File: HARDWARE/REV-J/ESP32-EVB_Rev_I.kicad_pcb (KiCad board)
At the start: 2 copper layers, 75.2 x 74.7 mm, 155 parts, among them CON1 TB3 DG306-5.0-3P, CON2 TB3 DG306-5.0-3P, Q1 BC817-40(SOT23), Q2 BC817-40(SOT23), Q3 Q12MHz/20pF/30ppm/2P/HC-49SM(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, Q4 BC817-40(SOT23), Q5 BC817-40(SOT23), Q7 BC817-40(SOT23), U1 BL4054B-42TPRN(SOT23-5), U10 BAT54C(SOT23-3), U2 SY8089AAAC(SOT23-5), U3 ESP-WROOM-32, U4 LAN8710A-EZC(QFN32), U5 CH340T(SSOP20W), U6 MCP2562-E/SN(SOIC-8_150mil), U7 RPM7236-H8, U8 NCP303LSN27T1G(SOT-23-5), U9 BAT54C(SOT23-3)

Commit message: Update 434121043836 (rev1).stp, 5040771891.stp, and 173 more files...
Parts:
- removed C/M: Closed(1-2)/Opened(2-3), OLIMEX_Jumpers-FP:SJ_2_SMALL_12_TIED
- added 5.0V/3.3V2: Closed(1-2)/Opened(2-3), OLIMEX_Jumpers-FP:SJ_2_SMALL_12_TIED, F.Cu at (127.4, 114.0)
- CAN_T1: moved to F.Cu
- R47: moved to B.Cu
- moved 5.0V/3.3V1 4.40 mm to (119.9, 112.8), turned to 180 degrees
- moved R13 2.99 mm to (133.3, 109.7), turned to 270 degrees
- moved CAN_T1 1.74 mm to (134.3, 112.6)
- moved R12 1.49 mm to (134.2, 114.8), turned to 180 degrees
- moved R47 1.30 mm to (135.5, 112.7)
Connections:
- 5.0V/3.3V1 pad 2: Net-(5.0V/3.3V1-Pad2) -> mb+
- C25 pad 2: Net-(5.0V/3.3V1-Pad2) -> mb+
- C26 pad 2: Net-(5.0V/3.3V1-Pad2) -> mb+
- R12 pad 1: GND -> /CANH
- R12 pad 2: /CANH -> GND
- R13 pad 1: /CANL -> mb+
- R13 pad 2: vm -> /CANL
- R48 pad 1: vm -> mb+
- R48 pad 2: Net-(5.0V/3.3V1-Pad2) -> mb+
- R49 pad 1: vm -> mb+
- U6 pad 2: GND -> Net-(U6-Pad2)
- U6 pad 3: Net-(5.0V/3.3V1-Pad2) -> Net-(U6-Pad2)
- U6 pad 8: vm -> mb+
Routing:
- net mb+: track 0.00 -> 26.3 mm, vias 0 -> 3
- net Net-(5.0V/3.3V1-Pad2): track 13.0 -> 0.00 mm, vias 1 -> 0
- net Net-(U6-Pad2): track 0.00 -> 8.96 mm
- net GND: track 995.9 -> 1002.4 mm, vias 133 -> 132
- net vm: track 5.82 -> 0.00 mm
- net /CANL: track 18.9 -> 22.5 mm, vias 1 -> 0
- net /GPI35/CAN-RX: track 111.3 -> 114.6 mm
- net +5V: track 140.2 -> 138.0 mm
- net Net-(5.0V/3.3V2-Pad2): track 3.97 -> 2.22 mm
- net +3V3: track 246.0 -> 244.3 mm, vias 15 -> 14
- net /CANH: track 27.0 -> 25.9 mm

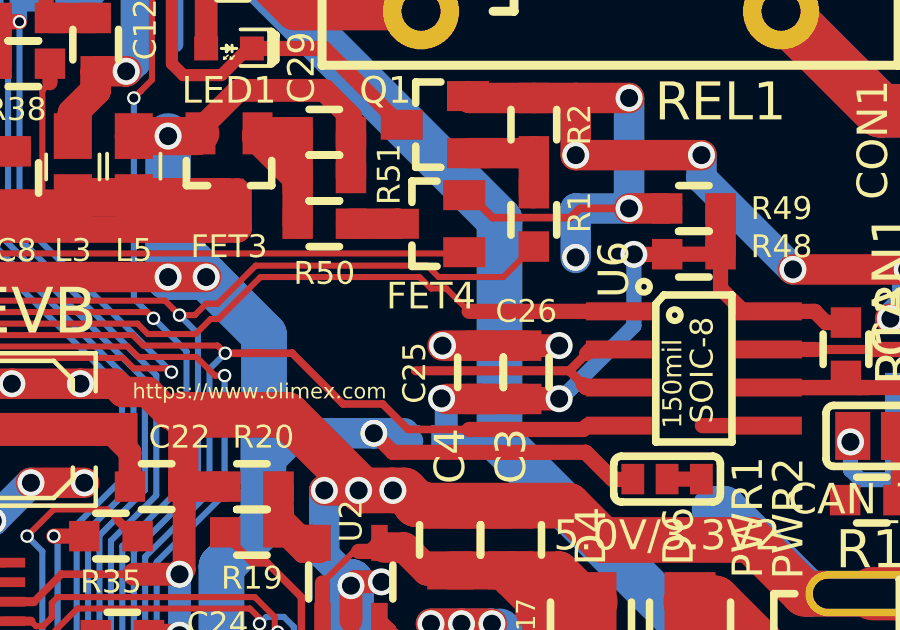
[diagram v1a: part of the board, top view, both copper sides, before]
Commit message: Update ESP32-EVB_Rev_I-cache.lib, ESP32-EVB_Rev_I.kicad_pcb, and 3 more files...
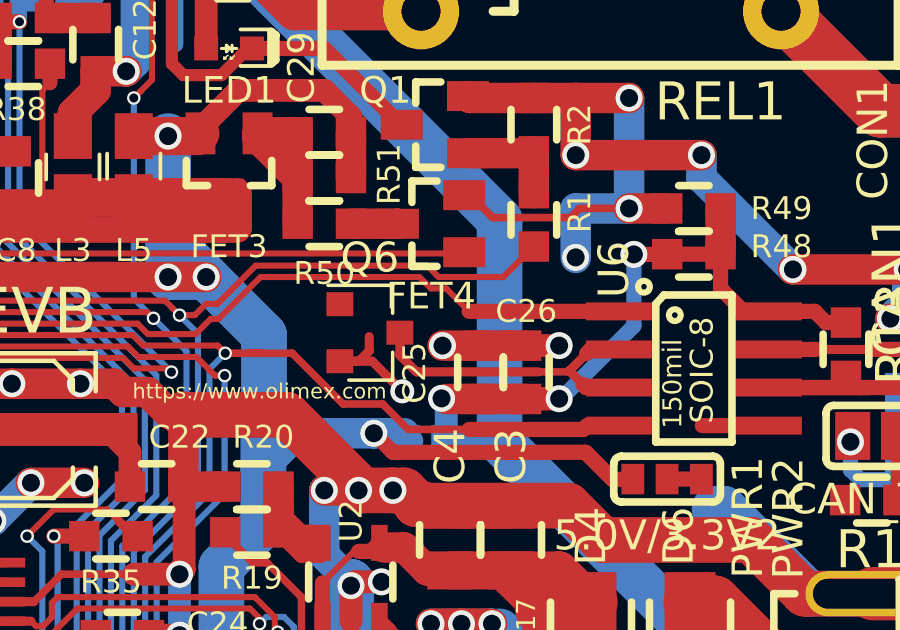
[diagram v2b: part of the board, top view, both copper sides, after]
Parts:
- added Q6: BC817, Package_TO_SOT_SMD:SOT-23, F.Cu at (117.5, 109.2)
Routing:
- net GND: track 1002.4 -> 1006.5 mm, vias 132 -> 133
- net Net-(Q6-Pad3): track 8.96 -> 10.5 mm

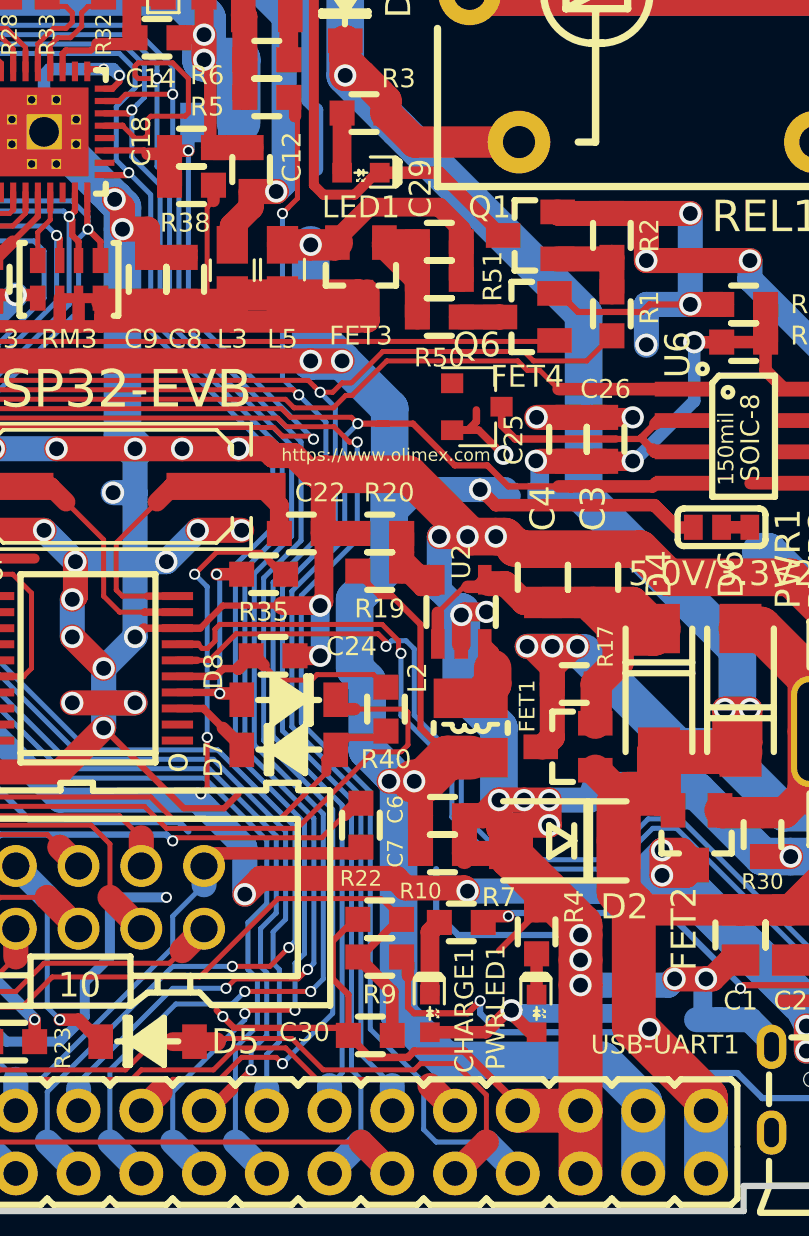
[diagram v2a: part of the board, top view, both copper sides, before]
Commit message: fix auto control flow modbus
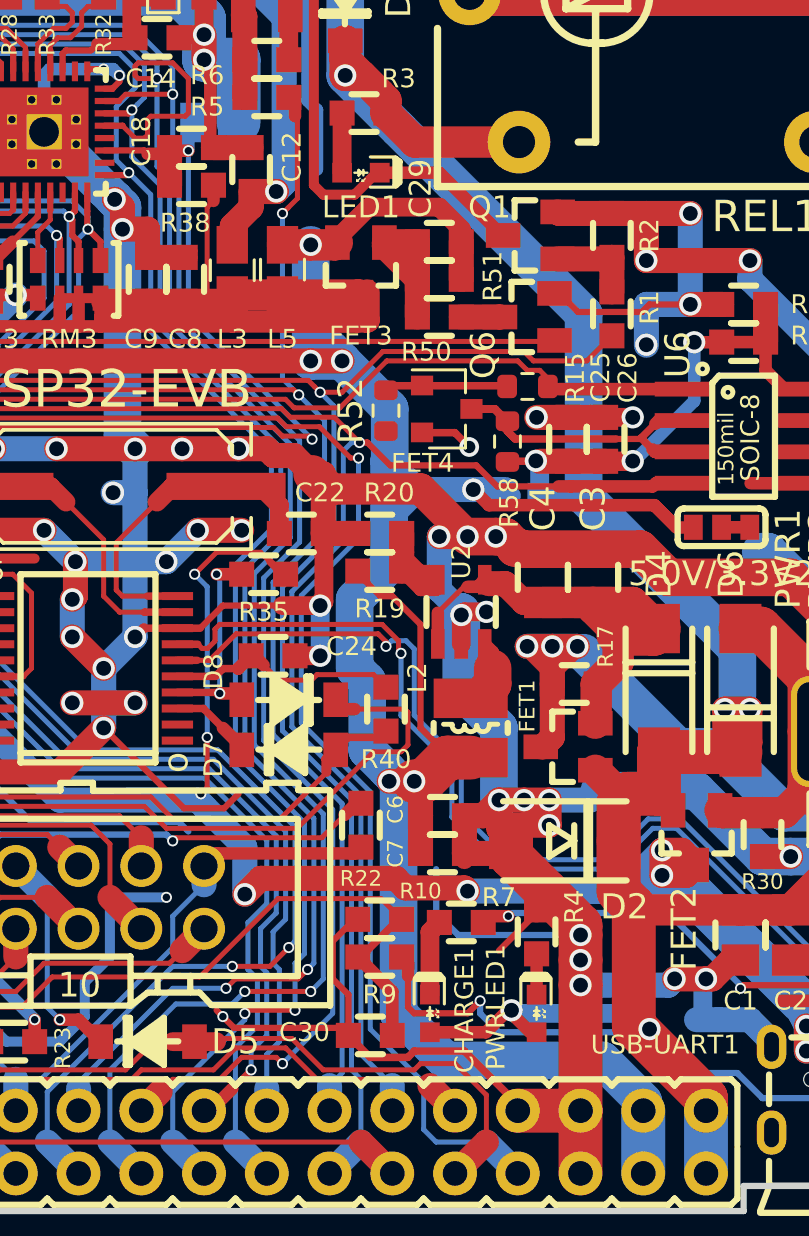
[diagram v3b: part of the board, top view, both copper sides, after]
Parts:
- added R15: R, Resistor_SMD:R_0603_1608Metric, F.Cu at (119.5, 108.3)
- added R52: R, Resistor_SMD:R_0603_1608Metric, F.Cu at (113.8, 109.3)
- added R58: R, Resistor_SMD:R_0603_1608Metric, F.Cu at (118.7, 110.6)
- moved Q6 1.22 mm to (116.2, 109.3)
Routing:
- net Net-(Q6-Pad1): track 0.00 -> 4.72 mm
- net Net-(Q6-Pad3): track 10.5 -> 14.7 mm
- net /GPI35/CAN-RX: track 114.6 -> 112.8 mm
- net GND: track 1006.5 -> 1005.0 mm
- net mb+: track 26.3 -> 27.5 mm
- net /GPIO5/CAN-TX: track 109.7 -> 110.3 mm

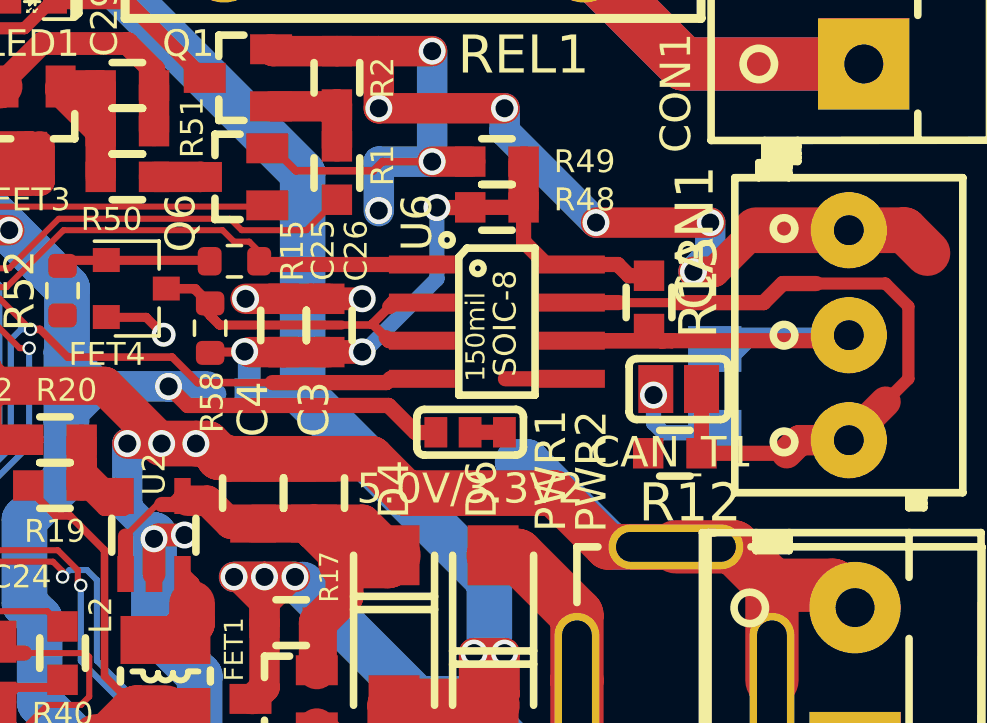
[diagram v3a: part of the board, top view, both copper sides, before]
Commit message: done modbus 485
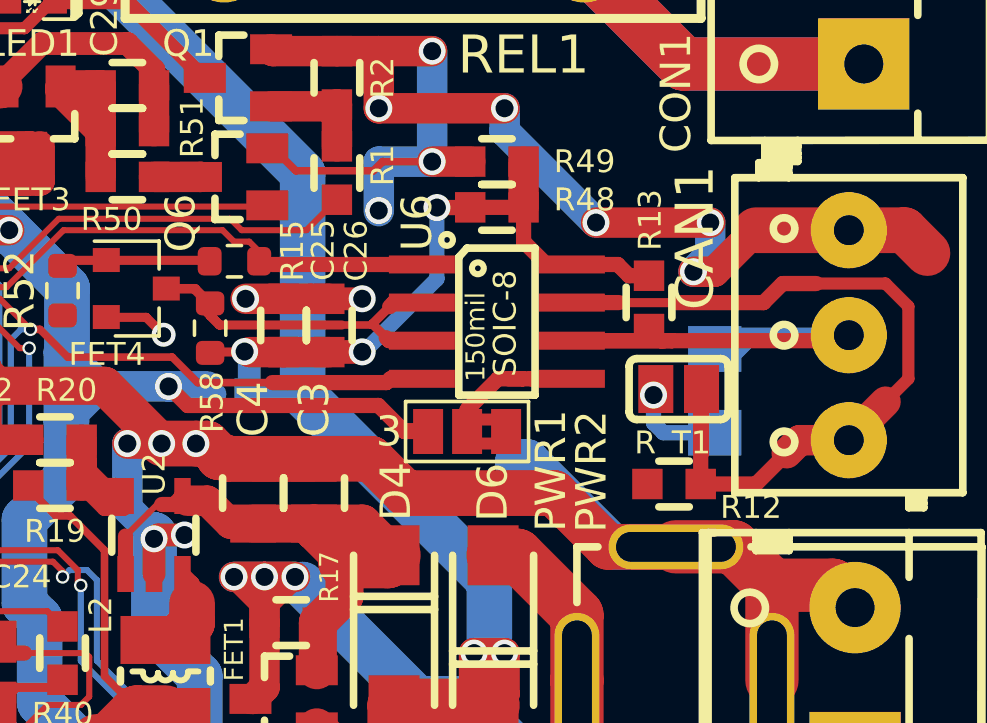
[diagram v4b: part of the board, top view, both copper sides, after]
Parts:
- removed 5.0V/3.3V2: Closed(1-2)/Opened(2-3), OLIMEX_Jumpers-FP:SJ_2_SMALL_12_TIED
- removed CAN_T1: Opened, OLIMEX_Jumpers-FP:SJ
- added JP1: SolderJumper_3_Bridged12, Jumper:SolderJumper-3_P1.3mm_Bridged2Bar12_Pad1.0x1.5mm_NumberLabels, F.Cu at (127.3, 114.0)
- added R_T1: Opened, OLIMEX_Jumpers-FP:SJ, F.Cu at (134.3, 112.6)
- moved R12 1.03 mm to (134.2, 115.8)
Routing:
- net /CANH: track 25.9 -> 30.1 mm
- net Net-(JP1-Pad2): track 2.22 -> 5.14 mm
- net +3V3: track 244.6 -> 243.8 mm

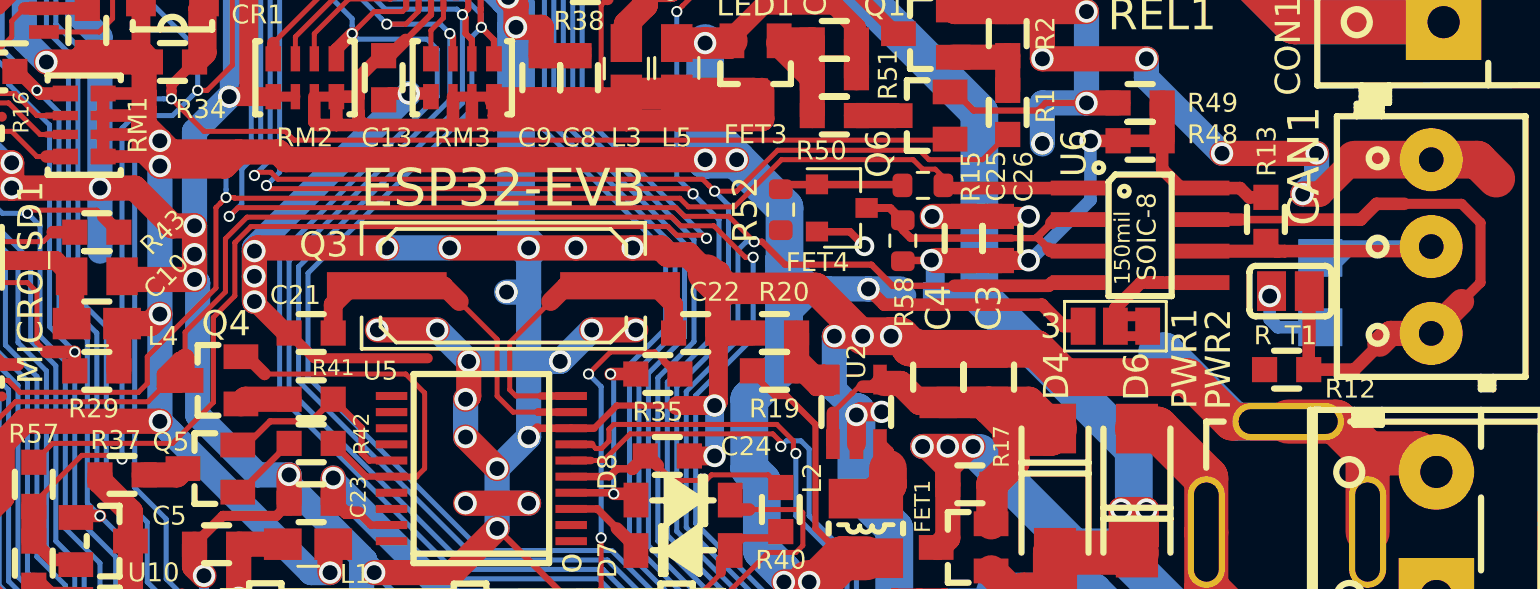
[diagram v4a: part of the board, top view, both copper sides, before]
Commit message: re-position micro usb port
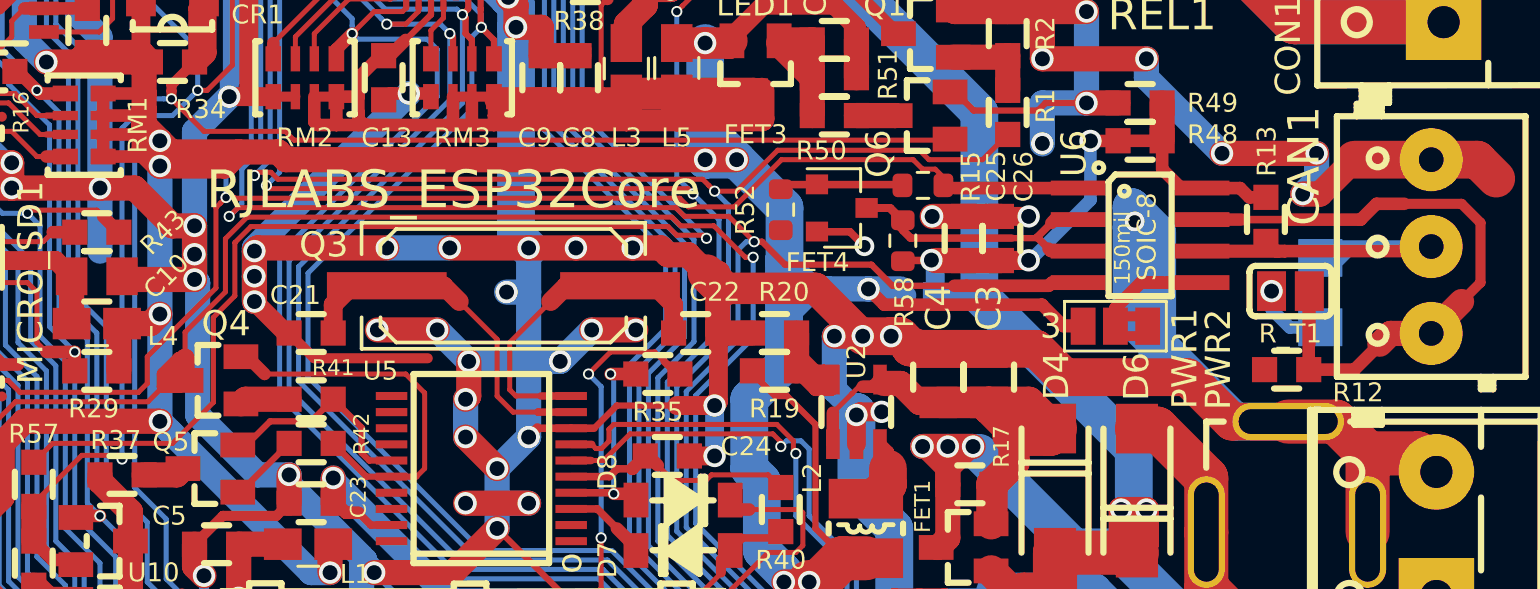
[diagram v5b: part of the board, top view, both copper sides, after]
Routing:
- net GND: track 1005.0 -> 1017.3 mm, vias 133 -> 134
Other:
- board text added: "RJLABS_ESP32Core"
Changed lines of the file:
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@@
     (thickness 1.6)
     (drawings 140)
-    (tracks 3314)
+    (tracks 3319)
     (zones 0)
     (modules 159)
@@
     (attr smd)
     (fp_text reference R52 (at 0 -1.43 90) (layer F.SilkS)
-      (effects (font (size 1 1) (thickness 0.15)))
+      (effects (font (size 0.762 0.762) (thickness 0.15)))
     )
     (fp_text value R (at 0 1.43 90) (layer F.Fab)
@@
     (tags "resistor 0603")
     (attr smd)
-    (fp_text reference R12 (at -2.564 -0.775) (layer F.SilkS)
+    (fp_text reference R12 (at -2.875 -0.925 180) (layer F.SilkS)
       (effects (font (size 0.762 0.762) (thickness 0.1905)))
     )
@@
     (tags "SOLDER JUMPER")
     (attr smd)
-    (fp_text reference R_T1 (at -0.203 1.79) (layer F.SilkS)
+    (fp_text reference R_T1 (at -0.003 1.715) (layer F.SilkS)
       (effects (font (size 0.762 0.762) (thickness 0.1905)))
     )
@@
   (gr_line (start 128.27 141.732) (end 128.27 140.716) (angle 90) (layer Edge.Cuts) (width 0.254))
   (gr_line (start 69.596 141.732) (end 128.27 141.732) (angle 90) (layer Edge.Cuts) (width 0.254))
-  (gr_text ESP32-EVB (at 102.616 108.458) (layer F.SilkS)
+  (gr_text RJLABS_ESP32Core (at 100.6 108.525) (layer F.SilkS)
     (effects (font (size 1.524 1.524) (thickness 0.381)))
   )
@@
   (via (at 134.82 108.7) (size 0.9) (drill 0.6) (layers F.Cu B.Cu) (net 2))
   (segment (start 135.382 108.138) (end 134.82 108.7) (width 1.016) (layer B.Cu) (net 2))
-  (segment (start 129.264 115.04) (end 128.96 115.04) (width 1.524) (layer B.Cu) (net 2))
-  (segment (start 134.237 117.869) (end 132.093 117.869) (width 1.524) (layer B.Cu) (net 2))
-  (segment (start 132.093 117.869) (end 129.264 115.04) (width 1.524) (layer B.Cu) (net 2))
   (segment (start 119.268512 114.935) (end 124.079 114.935) (width 1.524) (layer F.Cu) (net 2))
   (segment (start 119.217703 114.884191) (end 119.268512 114.935) (width 1.524) (layer F.Cu) (net 2))
@@
   (segment (start 116.58 110.22) (end 117.16 110.8) (width 0.3048) (layer F.Cu) (net 2))
   (segment (start 115.28 110.22) (end 116.58 110.22) (width 0.3048) (layer F.Cu) (net 2))
+  (segment (start 127.925 109.225) (end 128.96 110.26) (width 1.524) (layer B.Cu) (net 2))
+  (segment (start 128.96 110.26) (end 128.96 115.04) (width 1.524) (layer B.Cu) (net 2))
+  (segment (start 127.925 113.701) (end 127.925 110.05) (width 1.524) (layer B.Cu) (net 2))
+  (segment (start 132.093 117.869) (end 127.925 113.701) (width 1.524) (layer B.Cu) (net 2))
+  (segment (start 134.237 117.869) (end 132.093 117.869) (width 1.524) (layer B.Cu) (net 2))
+  (segment (start 127.925 110.05) (end 127.925 109.225) (width 1.524) (layer B.Cu) (net 2))
+  (via (at 128.05 109.8) (size 0.8) (drill 0.5) (layers F.Cu B.Cu) (net 2))
   (segment (start 139.94638 129.53238) (end 136.017 125.603) (width 1.524) (layer B.Cu) (net 3))
   (segment (start 136.017 125.603) (end 129.921 125.603) (width 1.524) (layer B.Cu) (net 3))
@@
   (segment (start 136.905 115.775) (end 138.365 114.315) (width 0.508) (layer F.Cu) (net 64))
   (segment (start 135.064 115.775) (end 136.905 115.775) (width 0.508) (layer F.Cu) (net 64))
-  (via (at 133.49 112.81) (size 0.9) (drill 0.6) (layers F.Cu B.Cu) (net 65))
-  (segment (start 133.49 112.81) (end 133.49 113.74) (width 0.508) (layer B.Cu) (net 65))
-  (segment (start 133.817 114.067) (end 135.53 114.067) (width 0.508) (layer B.Cu) (net 65))
-  (segment (start 133.49 113.74) (end 133.817 114.067) (width 0.508) (layer B.Cu) (net 65))
+  (via (at 133.566 112.609996) (size 0.9) (drill 0.6) (layers F.Cu B.Cu) (net 65))
+  (segment (start 133.566 113.341) (end 133.566 112.609996) (width 0.508) (layer B.Cu) (net 65))
+  (segment (start 134.3 114.075) (end 133.566 113.341) (width 0.508) (layer B.Cu) (net 65))
+  (segment (start 135.522 114.075) (end 134.3 114.075) (width 0.508) (layer B.Cu) (net 65))
+  (segment (start 135.53 114.067) (end 135.522 114.075) (width 0.508) (layer B.Cu) (net 65))
   (via (at 73.025 132.08) (size 0.45) (drill 0.3) (layers F.Cu B.Cu) (net 66))
   (segment (start 105.156 134.874) (end 104.389 134.874) (width 0.2032) (layer F.Cu) (net 66))
@@
     (connect_pads (clearance 0.381))
     (min_thickness 0.254)
-    (fill yes (arc_segments 16) (thermal_gap 0.508) (thermal_bridge_width 0.635))
+    (fill (arc_segments 16) (thermal_gap 0.508) (thermal_bridge_width 0.635))
     (polygon
       (pts
@@
     (connect_pads (clearance 0.381))
     (min_thickness 0.254)
-    (fill yes (arc_segments 16) (thermal_gap 0.508) (thermal_bridge_width 0.635))
+    (fill (arc_segments 16) (thermal_gap 0.508) (thermal_bridge_width 0.635))
     (polygon
       (pts
@@
     (connect_pads (clearance 0.254))
     (min_thickness 0.254)
-    (fill yes (arc_segments 16) (thermal_gap 0.508) (thermal_bridge_width 1.27))
+    (fill (arc_segments 16) (thermal_gap 0.508) (thermal_bridge_width 1.27))
     (polygon
       (pts
@@
     (connect_pads (clearance 0.381))
     (min_thickness 0.254)
-    (fill yes (arc_segments 16) (thermal_gap 0.508) (thermal_bridge_width 1.27))
+    (fill (arc_segments 16) (thermal_gap 0.508) (thermal_bridge_width 1.27))
     (polygon
       (pts
